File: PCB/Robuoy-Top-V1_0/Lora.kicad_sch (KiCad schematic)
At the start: 5 parts, among them J601 Conn_Coaxial, U601 Ai-Thinker-Ra-01

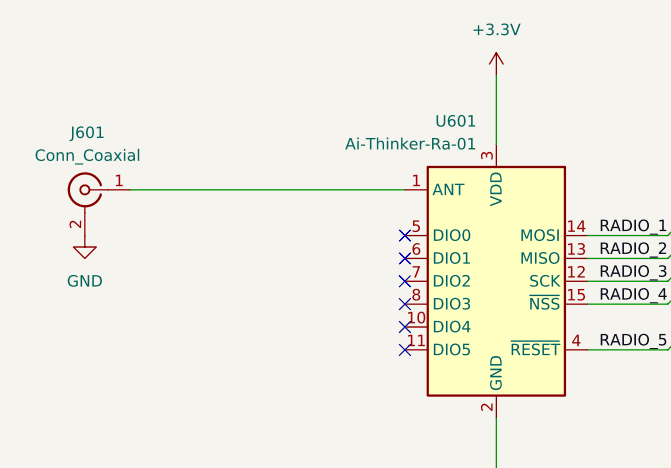
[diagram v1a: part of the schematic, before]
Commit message: Sub ready for routing
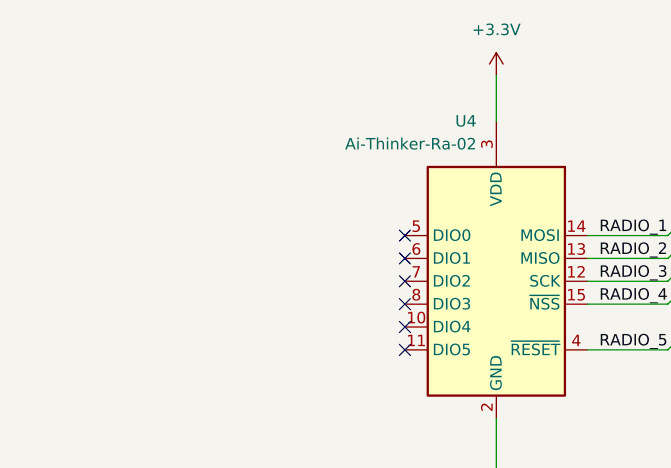
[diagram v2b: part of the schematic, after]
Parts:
- removed J601: Conn_Coaxial, Connector_Coaxial:U.FL_Hirose_U.FL-R-SMT-1_Vertical, symbol Connector:Conn_Coaxial
- removed U601: Ai-Thinker-Ra-01, RF_Module:Ai-Thinker-Ra-01-LoRa, symbol RF_Module:Ai-Thinker-Ra-01
- added U4: Ai-Thinker-Ra-02, RF_Module:Ai-Thinker-Ra-01-LoRa, symbol RF_Module:Ai-Thinker-Ra-02
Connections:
- net +3.3V: now also U4.3 (VDD)
- net GND: now also U4.1 (GND), U4.16 (GND), U4.2 (GND), U4.9 (GND)
- net RADIO_1: now also U4.14 (MOSI)
- net RADIO_2: now also U4.13 (MISO)
- net RADIO_3: now also U4.12 (SCK)
- net RADIO_4: now also U4.15 (~{NSS})
- net RADIO_5: now also U4.4 (~{RESET})
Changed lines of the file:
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@@
-		)
-	)
-	(wire
-		(pts
-			(xy 102.87 86.36) (xy 133.35 86.36)
-		)
-		(stroke
-			(width 0)
-			(type default)
 		)
 	)
@@
 	(wire
 		(pts
-			(xy 143.51 73.66) (xy 143.51 81.28)
+			(xy 143.51 73.66) (xy 143.51 78.74)
 		)
 		(stroke
@@
 	)
 	(symbol
+		(lib_id "RF_Module:Ai-Thinker-Ra-02")
+		(at 143.51 96.52 0)
+		(mirror y)
+		(unit 1)
+		(exclude_from_sim no)
+		(in_bom yes)
+		(on_board yes)
+		(dnp no)
+		(property "Reference" "U4"
+			(at 141.3159 78.74 0)
+			(effects
+				(font
+					(size 1.27 1.27)
+				)
+				(justify left)
+			)
+		)
+		(property "Value" "Ai-Thinker-Ra-02"
+			(at 141.3159 81.28 0)
+			(effects
+				(font
+					(size 1.27 1.27)
+				)
+				(justify left)
+			)
+		)
+		(property "Footprint" "RF_Module:Ai-Thinker-Ra-01-LoRa"
+			(at 118.11 106.68 0)
+			(effects
+				(font
+					(size 1.27 1.27)
+				)
+				(hide yes)
+			)
+		)
+		(property "Datasheet" "http://wiki.ai-thinker.com/_media/lora/docs/c048ps01a1_ra-02_product_specification_v1.1.pdf"
+			(at 140.97 77.47 0)
+			(effects
+				(font
+					(size 1.27 1.27)
+				)
+				(hide yes)
+			)
+		)
+		(property "Description" "Ai-Thinker Ra-02 410-525 MHz LoRa Module, SPI interface, U.FL antenna connector"
+			(at 143.51 96.52 0)
+			(effects
+				(font
+					(size 1.27 1.27)
+				)
+				(hide yes)
+			)
+		)
+		(property "LCSC" "C90039"
+			(at 143.51 96.52 0)
+			(effects
+				(font
+					(size 1.27 1.27)
+				)
+				(hide yes)
+			)
+		)
+		(pin "9"
+		)
+		(pin "5"
+		)
+		(pin "14"
+		)
+		(pin "8"
+		)
+		(pin "12"
+		)
+		(pin "1"
+		)
+		(pin "7"
+		)
+		(pin "4"
+		)
+		(pin "11"
+		)
+		(pin "15"
+		)
+		(pin "6"
+		)
+		(pin "13"
+		)
+		(pin "16"
+		)
+		(pin "2"
+		)
+		(pin "3"
+		)
+		(pin "10"
+		)
+		(instances
+			(project "Robuoy-Top"
+				(path "/77bea089-a6ae-4a6f-b95b-7a9010ad7c5d/1dc26a2c-fbf5-4621-ae52-68ee3e95a03a"
+					(reference "U4")
+					(unit 1)
+				)
+			)
+		)
+	)
+	(symbol
 		(lib_id "power:+3.3V")
 		(at 143.51 73.66 0)
@@
 				(path "/77bea089-a6ae-4a6f-b95b-7a9010ad7c5d/1dc26a2c-fbf5-4621-ae52-68ee3e95a03a"
 					(reference "#PWR0604")
-					(unit 1)
-				)
-			)
-		)
-	)
-	(symbol
-		(lib_id "power:GND")
-		(at 97.79 91.44 0)
-		(unit 1)
-		(exclude_from_sim no)
-		(in_bom yes)
-		(on_board yes)
-		(dnp no)
-		(fields_autoplaced yes)
-		(property "Reference" "#PWR0601"
-			(at 97.79 97.79 0)
-			(effects
-				(font
-					(size 1.27 1.27)
-				)
-				(hide yes)
-			)
-		)
-		(property "Value" "GND"
-			(at 97.79 96.52 0)
-			(effects
-				(font
-					(size 1.27 1.27)
-				)
-			)
-		)
-		(property "Footprint" ""
-			(at 97.79 91.44 0)
-			(effects
-				(font
-					(size 1.27 1.27)
-				)
-				(hide yes)
-			)
-		)
-		(property "Datasheet" ""
-			(at 97.79 91.44 0)
-			(effects
-				(font
-					(size 1.27 1.27)
-				)
-				(hide yes)
-			)
-		)
-		(property "Description" ""
-			(at 97.79 91.44 0)
-			(effects
-				(font
-					(size 1.27 1.27)
-				)
-				(hide yes)
-			)
-		)
-		(pin "1"
-		)
-		(instances
-			(project "Robuoy-Top"
-				(path "/77bea089-a6ae-4a6f-b95b-7a9010ad7c5d/1dc26a2c-fbf5-4621-ae52-68ee3e95a03a"
-					(reference "#PWR0601")
 					(unit 1)
 				)
@@
 	)
 	(symbol
-		(lib_id "Connector:Conn_Coaxial")
-		(at 97.79 86.36 0)
-		(mirror y)
-		(unit 1)
-		(exclude_from_sim no)
-		(in_bom yes)
-		(on_board yes)
-		(dnp no)
-		(fields_autoplaced yes)
-		(property "Reference" "J601"
-			(at 98.1074 80.01 0)
-			(effects
-				(font
-					(size 1.27 1.27)
-				)
-			)
-		)
-		(property "Value" "Conn_Coaxial"
-			(at 98.1074 82.55 0)
-			(effects
-				(font
-					(size 1.27 1.27)
-				)
-			)
-		)
-		(property "Footprint" "Connector_Coaxial:U.FL_Hirose_U.FL-R-SMT-1_Vertical"
-			(at 97.79 86.36 0)
-			(effects
-				(font
-					(size 1.27 1.27)
-				)
-				(hide yes)
-			)
-		)
-		(property "Datasheet" " ~"
-			(at 97.79 86.36 0)
-			(effects
-				(font
-					(size 1.27 1.27)
-				)
-				(hide yes)
-			)
-		)
-		(property "Description" ""
-			(at 97.79 86.36 0)
-			(effects
-				(font
-					(size 1.27 1.27)
-				)
-				(hide yes)
-			)
-		)
-		(property "LCSC" "C88374"
-			(at 98.1074 80.01 0)
-			(effects
-				(font
-					(size 1.27 1.27)
-				)
-				(hide yes)
-			)
-		)
-		(pin "1"
-		)
-		(pin "2"
-		)
-		(instances
-			(project "Robuoy-Top"
-				(path "/77bea089-a6ae-4a6f-b95b-7a9010ad7c5d/1dc26a2c-fbf5-4621-ae52-68ee3e95a03a"
-					(reference "J601")
-					(unit 1)
-				)
-			)
-		)
-	)
-	(symbol
 		(lib_id "Device:C_Small")
 		(at 128.905 180.34 0)
@@
 					(unit 1)
 				)
-			)
-		)
-	)
-	(symbol
-		(lib_id "RF_Module:Ai-Thinker-Ra-01")
-		(at 143.51 96.52 0)
-		(mirror y)
-		(unit 1)
-		(exclude_from_sim no)
-		(in_bom yes)
-		(on_board yes)
-		(dnp no)
-		(property "Reference" "U601"
-			(at 141.3159 78.74 0)
-			(effects
-				(font
-					(size 1.27 1.27)
-				)
-				(justify left)
-			)
-		)
-		(property "Value" "Ai-Thinker-Ra-01"
-			(at 141.3159 81.28 0)
-			(effects
-				(font
-					(size 1.27 1.27)
-				)
-				(justify left)
-			)
-		)
-		(property "Footprint" "RF_Module:Ai-Thinker-Ra-01-LoRa"
-			(at 118.11 106.68 0)
-			(effects
-				(font
-					(size 1.27 1.27)
-				)
-				(hide yes)
-			)
-		)
-		(property "Datasheet" "http://wiki.ai-thinker.com/_media/lora/docs/c047ps01a1_ra-01_product_specification_v1.1.pdf"
-			(at 140.97 78.74 0)
-			(effects
-				(font
-					(size 1.27 1.27)
-				)
-				(hide yes)
-			)
-		)
-		(property "Description" ""
-			(at 143.51 96.52 0)
-			(effects
-				(font
-					(size 1.27 1.27)
-				)
-				(hide yes)
-			)
-		)
-		(property "LCSC" "C90040"
-			(at 143.51 96.52 0)
-			(effects
-				(font
-					(size 1.27 1.27)
-				)
-				(hide yes)
-			)
-		)
-		(pin "1"
-		)
-		(pin "10"
-		)
-		(pin "11"
-		)
-		(pin "12"
-		)
-		(pin "13"
-		)
-		(pin "14"
-		)
-		(pin "15"
-		)
-		(pin "16"
-		)
-		(pin "2"
-		)
-		(pin "3"
-		)
-		(pin "4"
-		)
-		(pin "5"
-		)
-		(pin "6"
-		)
-		(pin "7"
-		)
-		(pin "8"
-		)
-		(pin "9"
-		)
-		(instances
-			(project "Robuoy-Top"
-				(path "/77bea089-a6ae-4a6f-b95b-7a9010ad7c5d/1dc26a2c-fbf5-4621-ae52-68ee3e95a03a"
-					(reference "U601")
-					(unit 1)
-				)

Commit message: gETTING READY FOR ROUTING
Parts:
- renumbered U4 to U301
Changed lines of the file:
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@@
 			(project "Robuoy-Top"
 				(path "/77bea089-a6ae-4a6f-b95b-7a9010ad7c5d/1dc26a2c-fbf5-4621-ae52-68ee3e95a03a"
-					(reference "C602")
+					(reference "C302")
 					(unit 1)
 				)
@@
 		(on_board yes)
 		(dnp no)
-		(property "Reference" "U4"
+		(property "Reference" "U301"
 			(at 141.3159 78.74 0)
 			(effects
@@
 			(project "Robuoy-Top"
 				(path "/77bea089-a6ae-4a6f-b95b-7a9010ad7c5d/1dc26a2c-fbf5-4621-ae52-68ee3e95a03a"
-					(reference "U4")
+					(reference "U301")
 					(unit 1)
 				)
@@
 		(dnp no)
 		(fields_autoplaced yes)
-		(property "Reference" "#PWR0604"
+		(property "Reference" "#PWR0303"
 			(at 143.51 77.47 0)
 			(effects
@@
 			(project "Robuoy-Top"
 				(path "/77bea089-a6ae-4a6f-b95b-7a9010ad7c5d/1dc26a2c-fbf5-4621-ae52-68ee3e95a03a"
-					(reference "#PWR0604")
+					(reference "#PWR0303")
 					(unit 1)
 				)
@@
 		(dnp no)
 		(fields_autoplaced yes)
-		(property "Reference" "#PWR0603"
+		(property "Reference" "#PWR0302"
 			(at 134.62 189.23 0)
 			(effects
@@
 			(project "Robuoy-Top"
 				(path "/77bea089-a6ae-4a6f-b95b-7a9010ad7c5d/1dc26a2c-fbf5-4621-ae52-68ee3e95a03a"
-					(reference "#PWR0603")
+					(reference "#PWR0302")
 					(unit 1)
 				)
@@
 			(project "Robuoy-Top"
 				(path "/77bea089-a6ae-4a6f-b95b-7a9010ad7c5d/1dc26a2c-fbf5-4621-ae52-68ee3e95a03a"
-					(reference "C601")
+					(reference "C301")
 					(unit 1)
 				)
@@
 		(dnp no)
 		(fields_autoplaced yes)
-		(property "Reference" "#PWR0602"
+		(property "Reference" "#PWR0301"
 			(at 134.62 181.61 0)
 			(effects
@@
 			(project "Robuoy-Top"
 				(path "/77bea089-a6ae-4a6f-b95b-7a9010ad7c5d/1dc26a2c-fbf5-4621-ae52-68ee3e95a03a"
-					(reference "#PWR0602")
+					(reference "#PWR0301")
 					(unit 1)
 				)
@@
 		(dnp no)
 		(fields_autoplaced yes)
-		(property "Reference" "#PWR0605"
+		(property "Reference" "#PWR0304"
 			(at 143.51 128.27 0)
 			(effects
@@
 			(project "Robuoy-Top"
 				(path "/77bea089-a6ae-4a6f-b95b-7a9010ad7c5d/1dc26a2c-fbf5-4621-ae52-68ee3e95a03a"
-					(reference "#PWR0605")
+					(reference "#PWR0304")
 					(unit 1)
 				)
@@
 			(project "Robuoy-Top"
 				(path "/77bea089-a6ae-4a6f-b95b-7a9010ad7c5d/1dc26a2c-fbf5-4621-ae52-68ee3e95a03a"
-					(reference "C603")
-					(unit 1)
-				)
+					(reference "C303")
+					(unit 1)
+				)

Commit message: Some more routing
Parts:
- U301: footprint RF_Module:Ai-Thinker-Ra-01-LoRa -> A_Module:Ai-Thinker-Ra-02-LoRa
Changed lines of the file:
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@@
 			)
 		)
-		(property "Footprint" "RF_Module:Ai-Thinker-Ra-01-LoRa"
+		(property "Footprint" "A_Module:Ai-Thinker-Ra-02-LoRa"
 			(at 118.11 106.68 0)
 			(effects

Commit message: print orderd by jlcpcb
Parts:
- C24: value 100u/16V -> 100u/10V; LCSC C90143 -> C23742
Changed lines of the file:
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@@
 			)
 		)
-		(property "Value" "100u/16V"
+		(property "Value" "100u/10V"
 			(at 116.205 184.15 0)
 			(effects
@@
 			)
 		)
-		(property "LCSC" "C90143"
+		(property "LCSC" "C23742"
 			(at 121.285 180.34 0)
 			(effects
@@
 			)
 		)
-		(property "Value" "100u/16V"
+		(property "Value" "100u/10V"
 			(at 105.41 184.15 0)
 			(effects
@@
 			)
 		)
-		(property "LCSC" "C90143"
+		(property "LCSC" "C23742"
 			(at 110.49 180.34 0)
 			(effects
